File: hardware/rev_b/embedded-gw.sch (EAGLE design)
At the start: 56 parts, among them J1 DM3BT-DSF-PEJS, J2 TC2030-JLINK-NL, J3 USB-A-MALE-PLUG, Q1 DMN32D2LDF, U1 AP7362A-33SP-13, U2 BT840X, U3 CP2102N-20, U4 ESDR0502N, U5 ESP32-WROVER-E, U6 ESP32-WROVER-E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

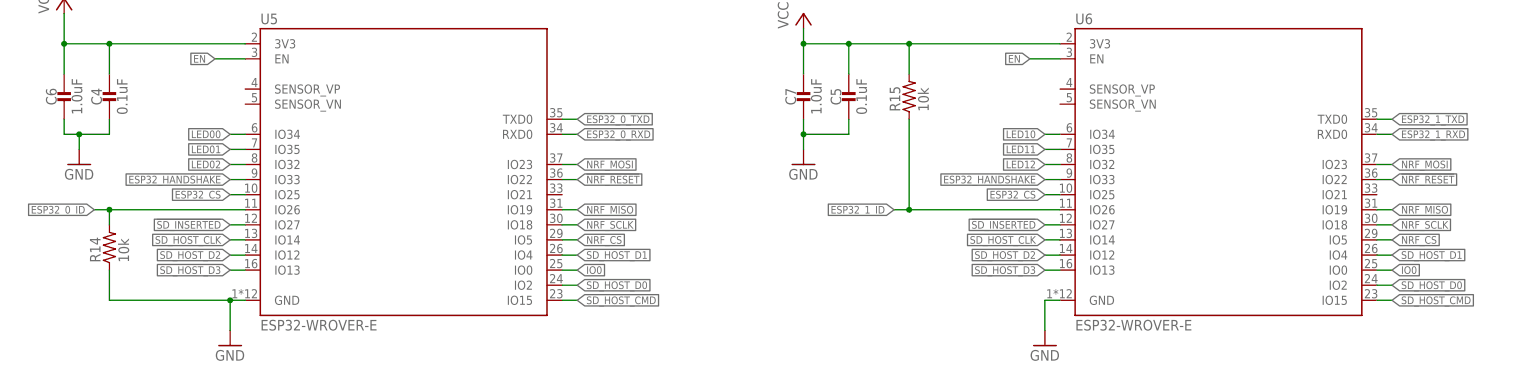
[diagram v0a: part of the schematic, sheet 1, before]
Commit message: Change handshake gpio from 33 to 21, add ipc
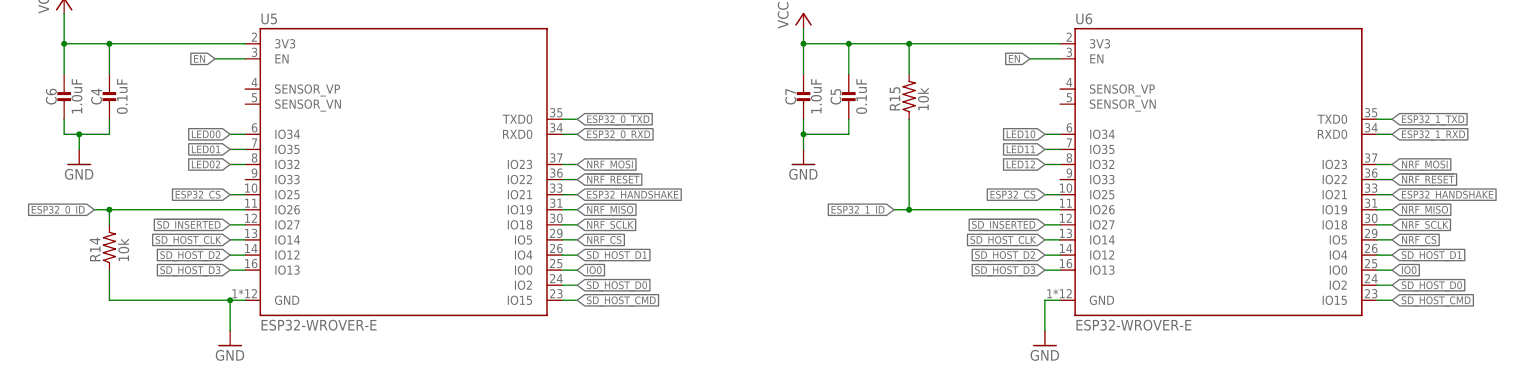
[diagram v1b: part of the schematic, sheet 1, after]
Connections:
- net ESP32_HANDSHAKE: now also U5.IO21, U6.IO21; no longer U5.IO33, U6.IO33
- net RXD: now also U3.TXD; no longer U3.RXD
- net TXD: now also U3.RXD; no longer U3.TXD
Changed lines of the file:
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@@
 <net name="ESP32_HANDSHAKE" class="0">
 <segment>
-<pinref part="U6" gate="G$1" pin="IO33"/>
-<wire x1="175.26" y1="147.32" x2="172.72" y2="147.32" width="0.1524" layer="91"/>
-<label x="172.72" y="147.32" size="1.27" layer="95" rot="R180" xref="yes"/>
-</segment>
-<segment>
-<pinref part="U5" gate="G$1" pin="IO33"/>
-<wire x1="38.1" y1="147.32" x2="35.56" y2="147.32" width="0.1524" layer="91"/>
-<label x="35.56" y="147.32" size="1.27" layer="95" rot="R180" xref="yes"/>
+<pinref part="U5" gate="G$1" pin="IO21"/>
+<wire x1="91.44" y1="144.78" x2="93.98" y2="144.78" width="0.1524" layer="91"/>
+<label x="93.98" y="144.78" size="1.27" layer="95" xref="yes"/>
+</segment>
+<segment>
+<pinref part="U6" gate="G$1" pin="IO21"/>
+<wire x1="228.6" y1="144.78" x2="231.14" y2="144.78" width="0.1524" layer="91"/>
+<label x="231.14" y="144.78" size="1.27" layer="95" xref="yes"/>
 </segment>
 </net>
@@
 <net name="RXD" class="0">
 <segment>
-<pinref part="U3" gate="G$1" pin="RXD"/>
-<wire x1="167.64" y1="96.52" x2="177.8" y2="96.52" width="0.1524" layer="91"/>
 <wire x1="177.8" y1="96.52" x2="177.8" y2="93.98" width="0.1524" layer="91"/>
 <pinref part="S3" gate="G$1" pin="I2"/>
 <wire x1="177.8" y1="93.98" x2="187.96" y2="93.98" width="0.1524" layer="91"/>
+<pinref part="U3" gate="G$1" pin="TXD"/>
+<wire x1="167.64" y1="99.06" x2="172.72" y2="99.06" width="0.1524" layer="91"/>
+<wire x1="172.72" y1="99.06" x2="175.26" y2="96.52" width="0.1524" layer="91"/>
+<wire x1="175.26" y1="96.52" x2="177.8" y2="96.52" width="0.1524" layer="91"/>
 </segment>
 </net>
 <net name="TXD" class="0">
 <segment>
-<pinref part="U3" gate="G$1" pin="TXD"/>
-<wire x1="167.64" y1="99.06" x2="177.8" y2="99.06" width="0.1524" layer="91"/>
 <wire x1="177.8" y1="99.06" x2="177.8" y2="104.14" width="0.1524" layer="91"/>
 <pinref part="S3" gate="G$1" pin="I1"/>
 <wire x1="177.8" y1="104.14" x2="187.96" y2="104.14" width="0.1524" layer="91"/>
-</segment>
-</net>
+<pinref part="U3" gate="G$1" pin="RXD"/>
+<wire x1="167.64" y1="96.52" x2="172.72" y2="96.52" width="0.1524" layer="91"/>
+<wire x1="172.72" y1="96.52" x2="175.26" y2="99.06" width="0.1524" layer="91"/>
+<wire x1="175.26" y1="99.06" x2="177.8" y2="99.06" width="0.1524" layer="91"/>
+</segment>
+</net>

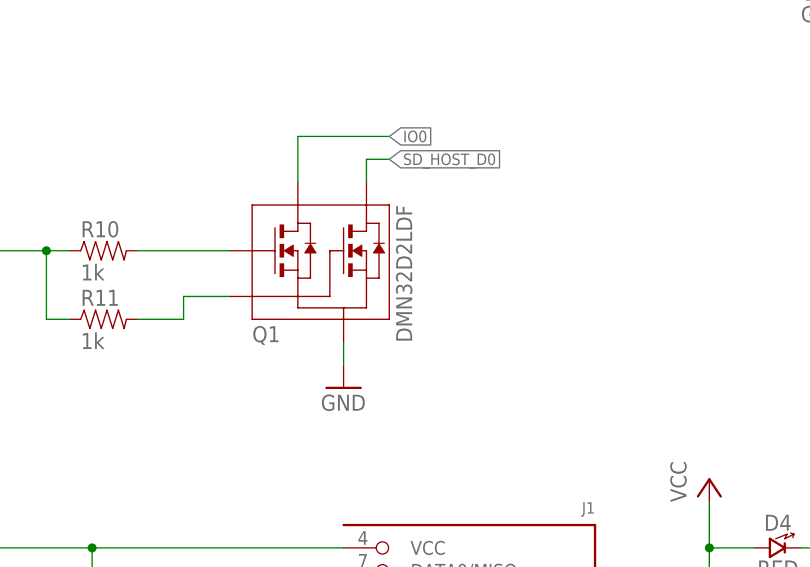
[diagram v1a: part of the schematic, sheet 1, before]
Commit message: Swap Q1 with QS5K2TR
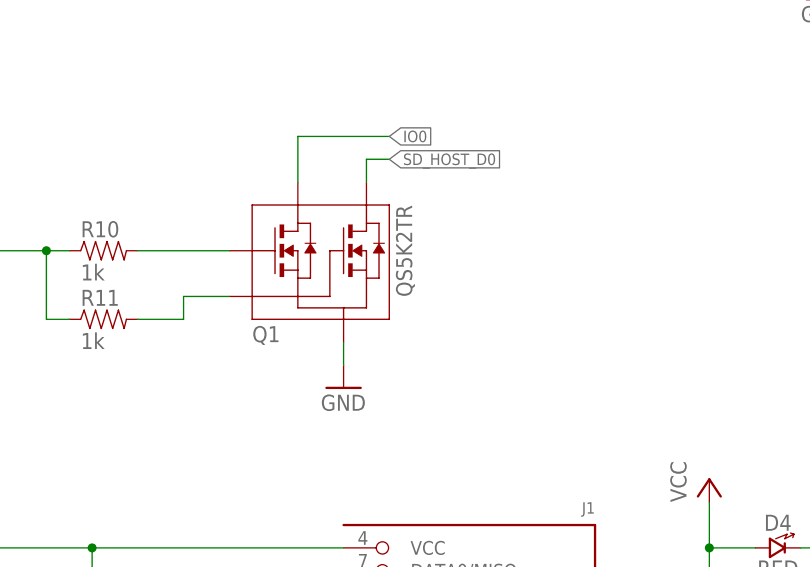
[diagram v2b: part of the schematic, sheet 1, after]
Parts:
- Q1: value DMN32D2LDF -> QS5K2TR; device fets:DMN32D2LDF -> fets:QS5K2TR
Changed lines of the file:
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@@
 <attribute name="MPN" value="RMCF0402JT1K00"/>
 </part>
-<part name="Q1" library="fets" deviceset="DMN32D2LDF" device=""/>
+<part name="Q1" library="fets" deviceset="QS5K2TR" device=""/>
 <part name="GND18" library="supply1" library_urn="urn:adsk.eagle:library:371" deviceset="GND" device=""/>
 <part name="P+8" library="supply1" library_urn="urn:adsk.eagle:library:371" deviceset="VCC" device=""/>
